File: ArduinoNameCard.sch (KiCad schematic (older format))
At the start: 24 parts, among them J1 Conn_01x05, J2 Conn_01x04, J3 Conn_01x06, J4 Conn_01x08, J5 Conn_01x06, SW1 SW_Push, U1 FT232RL, U2 MCU-ATMEGA328P-AU(TQFP32)

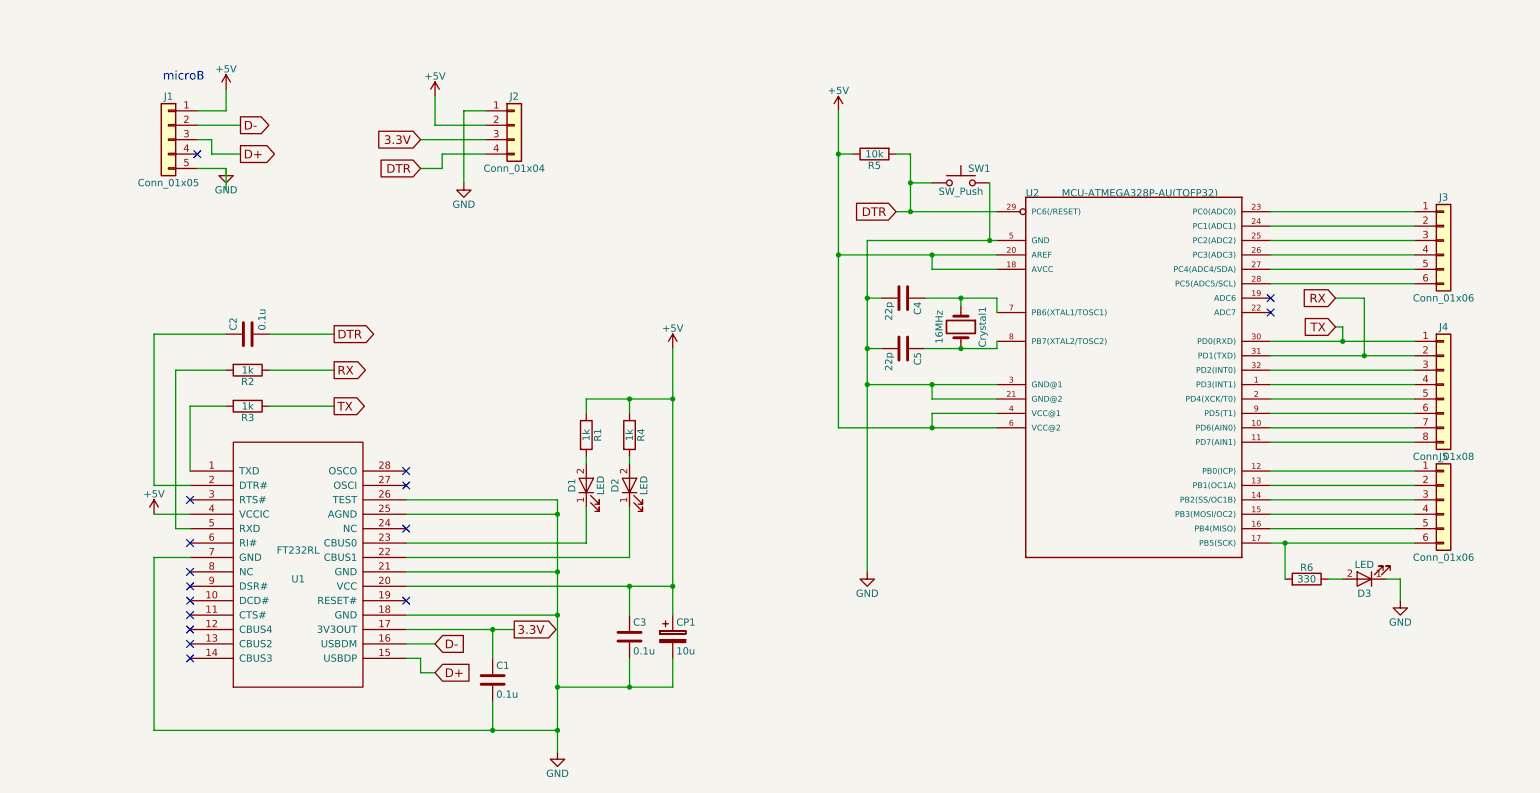
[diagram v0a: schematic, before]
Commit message: ・README.mdの追加 ・PCBの設計 諸変更を行った。
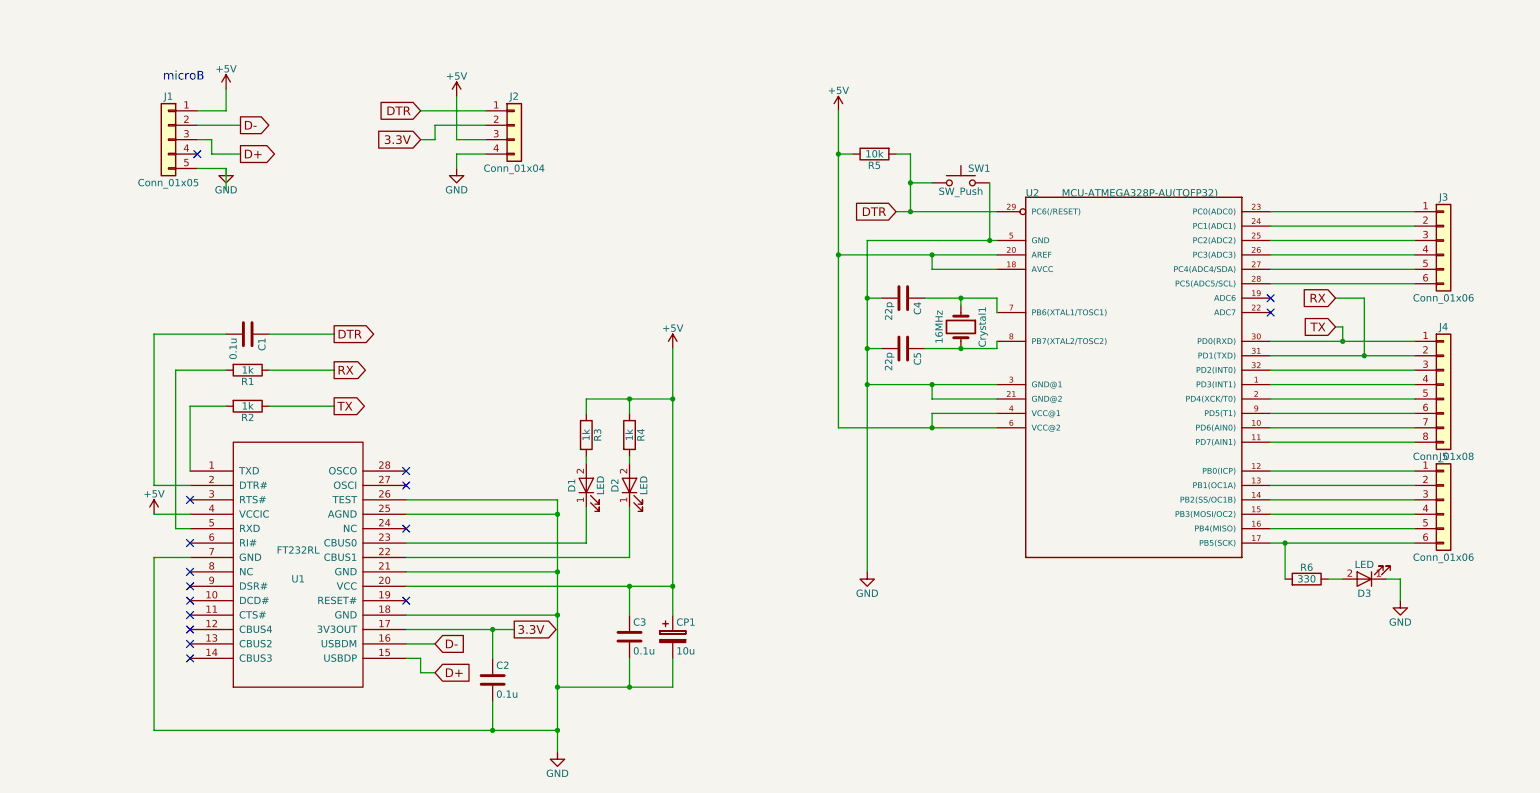
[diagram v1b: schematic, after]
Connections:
- net +5V: now also J2.3 (Pin_3), R3.1; no longer J2.2 (Pin_2), R1.1
- net 3.3V: now also C2.1, J2.2 (Pin_2); no longer C1.1, J2.3 (Pin_3)
- net DTR: now also C1.1, J2.1 (Pin_1); no longer C2.2, J2.4 (Pin_4)
- net GND: now also C2.2, J2.4 (Pin_4); no longer C1.2, J2.1 (Pin_1)
- net RX: now also R1.1; no longer R2.1
- net TX: now also R2.1; no longer R3.1
- net at U1.1 (TXD): now also R2.2; no longer R3.2
- net at U1.2 (DTR#): now also C1.2; no longer C2.1
- net at U1.5 (RXD): now also R1.2; no longer R2.2
- net at D1.2 (A): now also R3.2; no longer R1.2
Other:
- moved on the sheet: C1, C2, R1, R2, R3
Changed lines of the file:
@@
 L R R1
 U 1 1 598D7C3A
-P 4700 4200
-F 0 "R1" V 4780 4200 50  0000 C CNN
-F 1 "1k" V 4700 4200 50  0000 C CNN
-F 2 "Resistors_SMD:R_0805_HandSoldering" V 4630 4200 50  0001 C CNN
-F 3 "" H 4700 4200 50  0001 C CNN
-	1    4700 4200
-	1    0    0    -1
+P 2350 3750
+F 0 "R1" V 2430 3750 50  0000 C CNN
+F 1 "1k" V 2350 3750 50  0000 C CNN
+F 2 "Resistors_SMD:R_0805_HandSoldering" V 2280 3750 50  0001 C CNN
+F 3 "" H 2350 3750 50  0001 C CNN
+	1    2350 3750
+	0    1    1    0
 $EndComp
 $Comp
@@
 L C C1
 U 1 1 598D853B
-P 4050 5900
-F 0 "C1" H 4075 6000 50  0000 L CNN
-F 1 "0.1u" H 4075 5800 50  0000 L CNN
-F 2 "Capacitors_SMD:C_0805_HandSoldering" H 4088 5750 50  0001 C CNN
-F 3 "" H 4050 5900 50  0001 C CNN
-	1    4050 5900
-	1    0    0    -1
+P 2350 3500
+F 0 "C1" H 2375 3600 50  0000 L CNN
+F 1 "0.1u" H 2375 3400 50  0000 L CNN
+F 2 "Capacitors_SMD:C_0805_HandSoldering" H 2388 3350 50  0001 C CNN
+F 3 "" H 2350 3500 50  0001 C CNN
+	1    2350 3500
+	0    1    1    0
 $EndComp
 Text GLabel 4200 5550 2    60   Output ~ 0
@@
 L R R2
 U 1 1 598DA5A4
-P 2350 3750
-F 0 "R2" V 2430 3750 50  0000 C CNN
-F 1 "1k" V 2350 3750 50  0000 C CNN
-F 2 "Resistors_SMD:R_0805_HandSoldering" V 2280 3750 50  0001 C CNN
-F 3 "" H 2350 3750 50  0001 C CNN
-	1    2350 3750
-	0    1    1    0
-$EndComp
-$Comp
-L R R3
-U 1 1 598DA689
 P 2350 4000
-F 0 "R3" V 2430 4000 50  0000 C CNN
+F 0 "R2" V 2430 4000 50  0000 C CNN
 F 1 "1k" V 2350 4000 50  0000 C CNN
 F 2 "Resistors_SMD:R_0805_HandSoldering" V 2280 4000 50  0001 C CNN
@@
 $EndComp
 $Comp
+L R R3
+U 1 1 598DA689
+P 4700 4200
+F 0 "R3" V 4780 4200 50  0000 C CNN
+F 1 "1k" V 4700 4200 50  0000 C CNN
+F 2 "Resistors_SMD:R_0805_HandSoldering" V 4630 4200 50  0001 C CNN
+F 3 "" H 4700 4200 50  0001 C CNN
+	1    4700 4200
+	1    0    0    -1
+$EndComp
+$Comp
 L C C2
 U 1 1 598DA6BD
-P 2350 3500
-F 0 "C2" H 2375 3600 50  0000 L CNN
-F 1 "0.1u" H 2375 3400 50  0000 L CNN
-F 2 "Capacitors_SMD:C_0805_HandSoldering" H 2388 3350 50  0001 C CNN
-F 3 "" H 2350 3500 50  0001 C CNN
-	1    2350 3500
-	0    -1   -1   0
+P 4050 5900
+F 0 "C2" H 4075 6000 50  0000 L CNN
+F 1 "0.1u" H 4075 5800 50  0000 L CNN
+F 2 "Capacitors_SMD:C_0805_HandSoldering" H 4088 5750 50  0001 C CNN
+F 3 "" H 4050 5900 50  0001 C CNN
+	1    4050 5900
+	1    0    0    -1
 $EndComp
 NoConn ~ 1950 5450
@@
 L GND #PWR08
 U 1 1 5AC81876
-P 3850 2450
-F 0 "#PWR08" H 3850 2200 50  0001 C CNN
-F 1 "GND" H 3850 2300 50  0000 C CNN
-F 2 "" H 3850 2450 50  0001 C CNN
-F 3 "" H 3850 2450 50  0001 C CNN
-	1    3850 2450
+P 3800 2350
+F 0 "#PWR08" H 3800 2100 50  0001 C CNN
+F 1 "GND" H 3800 2200 50  0000 C CNN
+F 2 "" H 3800 2350 50  0001 C CNN
+F 3 "" H 3800 2350 50  0001 C CNN
+	1    3800 2350
 	1    0    0    -1
 $EndComp
@@
 L +5V #PWR09
 U 1 1 5AC818BA
-P 3650 1850
-F 0 "#PWR09" H 3650 1700 50  0001 C CNN
-F 1 "+5V" H 3650 1990 50  0000 C CNN
-F 2 "" H 3650 1850 50  0001 C CNN
-F 3 "" H 3650 1850 50  0001 C CNN
-	1    3650 1850
+P 3800 1850
+F 0 "#PWR09" H 3800 1700 50  0001 C CNN
+F 1 "+5V" H 3800 1990 50  0000 C CNN
+F 2 "" H 3800 1850 50  0001 C CNN
+F 3 "" H 3800 1850 50  0001 C CNN
+	1    3800 1850
 	1    0    0    -1
 $EndComp
@@
 	1    0    0    -1
 $EndComp
-Text GLabel 3550 2350 0    60   Input ~ 0
+Text GLabel 3550 1950 0    60   Input ~ 0
 DTR
 Wire Wire Line
-	7050 3250 7300 3250
-Wire Wire Line
-	7300 3250 7550 3250
+	7050 3250 7550 3250
 Wire Wire Line
 	7550 3250 7550 3350
@@
 	6950 2450 7100 2450
 Wire Wire Line
-	6950 2250 6950 2450
-Wire Wire Line
-	6950 2450 6950 2650
+	6950 2250 6950 2650
 Connection ~ 6450 2250
 Wire Wire Line
-	6450 1950 6450 2250
-Wire Wire Line
-	6450 2250 6450 2950
-Wire Wire Line
-	6450 2950 6450 4150
+	6450 1950 6450 4150
 Wire Wire Line
 	6450 2250 6550 2250
@@
 Connection ~ 6450 2950
 Wire Wire Line
-	6450 2950 7100 2950
-Wire Wire Line
-	7100 2950 7550 2950
-Wire Wire Line
-	6650 2850 7500 2850
-Wire Wire Line
-	7500 2850 7550 2850
+	6450 2950 7550 2950
+Wire Wire Line
+	6650 2850 7550 2850
 Connection ~ 7100 3850
 Wire Wire Line
@@
 	7550 3950 7100 3950
 Wire Wire Line
-	6650 2850 6650 3250
-Wire Wire Line
-	6650 3250 6650 3600
-Wire Wire Line
-	6650 3600 6650 3850
-Wire Wire Line
-	6650 3850 6650 5150
-Wire Wire Line
-	6650 3850 7100 3850
-Wire Wire Line
-	7100 3850 7550 3850
+	6650 2850 6650 5150
+Wire Wire Line
+	6650 3850 7550 3850
 Connection ~ 7100 4150
 Wire Wire Line
@@
 	7100 4150 7100 4050
 Wire Wire Line
-	6450 4150 7100 4150
-Wire Wire Line
-	7100 4150 7550 4150
-Wire Wire Line
-	6850 2650 6950 2650
-Wire Wire Line
-	6950 2650 7550 2650
+	6450 4150 7550 4150
+Wire Wire Line
+	6850 2650 7550 2650
 Wire Wire Line
 	1850 3750 2200 3750
@@
 Connection ~ 4050 5550
 Wire Wire Line
-	3450 5550 4050 5550
-Wire Wire Line
-	4050 5550 4200 5550
+	3450 5550 4200 5550
 Connection ~ 4050 6250
 Wire Wire Line
@@
 Connection ~ 4500 5950
 Wire Wire Line
-	4500 5950 5000 5950
-Wire Wire Line
-	5000 5950 5300 5950
+	4500 5950 5300 5950
 Wire Wire Line
 	5000 5750 5000 5950
@@
 Connection ~ 5000 3950
 Wire Wire Line
-	5300 5250 5000 5250
-Wire Wire Line
-	5000 5250 3450 5250
-Wire Wire Line
-	5300 3600 5300 3950
-Wire Wire Line
-	5300 3950 5300 5250
-Wire Wire Line
-	5300 5250 5300 5450
+	5300 5250 3450 5250
+Wire Wire Line
+	5300 3600 5300 5450
 Connection ~ 4500 6250
 Wire Wire Line
@@
 	4500 5150 3450 5150
 Wire Wire Line
-	1700 6250 4050 6250
-Wire Wire Line
-	4050 6250 4500 6250
-Wire Wire Line
-	4500 4650 4500 4750
-Wire Wire Line
-	4500 4750 4500 5150
-Wire Wire Line
-	4500 5150 4500 5450
-Wire Wire Line
-	4500 5450 4500 5950
-Wire Wire Line
-	4500 5950 4500 6250
-Wire Wire Line
-	4500 6250 4500 6400
+	4500 6250 1700 6250
+Wire Wire Line
+	4500 4650 4500 6400
 Wire Wire Line
 	4500 5450 3450 5450
@@
 	4700 3950 4700 4050
 Wire Wire Line
-	4700 3950 5000 3950
-Wire Wire Line
-	5000 3950 5300 3950
+	4700 3950 5300 3950
 Wire Wire Line
 	5000 4400 5000 4350
@@
 	7550 3600 7550 3550
 Wire Wire Line
-	7050 3600 7300 3600
-Wire Wire Line
-	7300 3600 7550 3600
+	7050 3600 7550 3600
 Wire Wire Line
 	7300 3300 7300 3250
@@
 Connection ~ 6650 3600
 Wire Wire Line
-	9450 3550 9950 3550
-Wire Wire Line
-	9950 3550 10450 3550
-Wire Wire Line
-	9450 3650 10100 3650
-Wire Wire Line
-	10100 3650 10450 3650
+	9450 3550 10450 3550
+Wire Wire Line
+	9450 3650 10450 3650
 Wire Wire Line
 	9450 3750 10450 3750
@@
 Wire Wire Line
 	10450 3150 9450 3150
-Wire Wire Line
-	3850 1950 4000 1950
-Wire Wire Line
-	3650 2050 4000 2050
-Wire Wire Line
-	3550 2150 4000 2150
 Connection ~ 7300 3600
 Wire Wire Line
@@
 Connection ~ 6650 3850
 Wire Wire Line
-	3650 2050 3650 1850
-Wire Wire Line
-	3850 1950 3850 2450
-Wire Wire Line
-	9450 4950 9550 4950
-Wire Wire Line
-	9550 4950 10450 4950
+	9450 4950 10450 4950
 Wire Wire Line
 	9550 4950 9550 5200
@@
 	10250 5200 10350 5200
 Wire Wire Line
-	4000 2250 3700 2250
-Wire Wire Line
-	3700 2250 3700 2350
-Wire Wire Line
-	3700 2350 3550 2350
+	4000 2250 3800 2250
+Wire Wire Line
+	3800 2250 3800 2350
 Wire Wire Line
 	6850 2250 6950 2250
@@
 	1    0    0    -1
 $EndComp
+Wire Wire Line
+	3550 1950 4000 1950
+Wire Wire Line
+	3550 2150 3650 2150
+Wire Wire Line
+	3650 2150 3650 2050
+Wire Wire Line
+	3650 2050 4000 2050
+Wire Wire Line
+	4000 2150 3800 2150
+Wire Wire Line
+	3800 2150 3800 1850
 $EndSCHEMATC

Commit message: 回路にヒューズを追加した
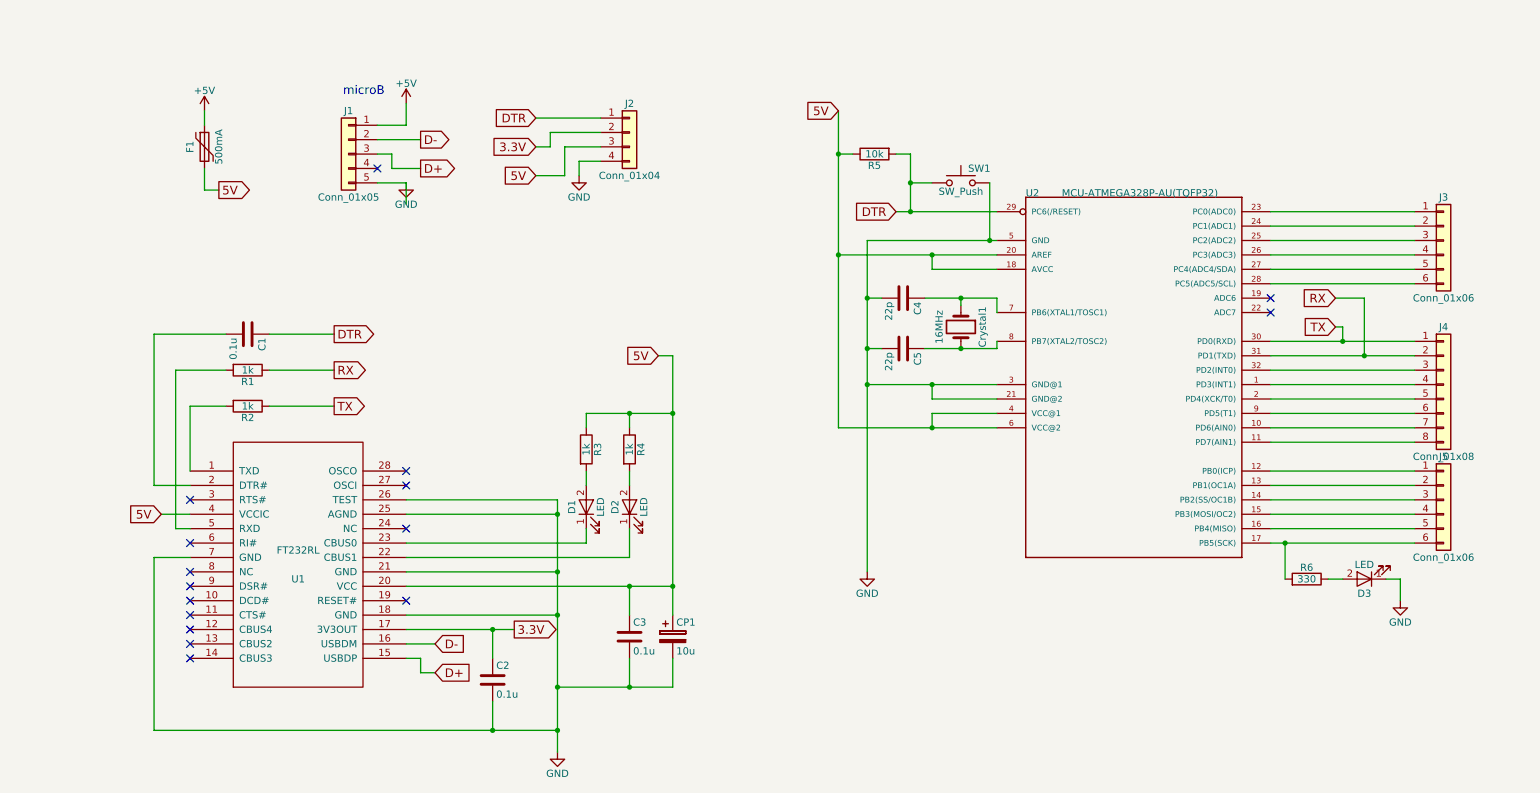
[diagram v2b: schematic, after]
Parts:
- added F1: 500mA, SMD_Packages:SMD-1210_Pol, symbol Polyfuse
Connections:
- net +5V: now also F1.1; no longer C3.1, CP1.1, J2.3 (Pin_3), R3.1, R4.1, R5.1, U1.20 (VCC), U1.4 (VCCIC), U2.18 (AVCC), U2.20 (AREF), U2.4 (VCC@1), U2.6 (VCC@2)
- new net 5V: C3.1, CP1.1, F1.2, J2.3 (Pin_3), R3.1, R4.1, R5.1, U1.20 (VCC), U1.4 (VCCIC), U2.18 (AVCC), U2.20 (AREF), U2.4 (VCC@1), U2.6 (VCC@2)
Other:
- moved on the sheet: D1, D2, J1, J2, R3, R4

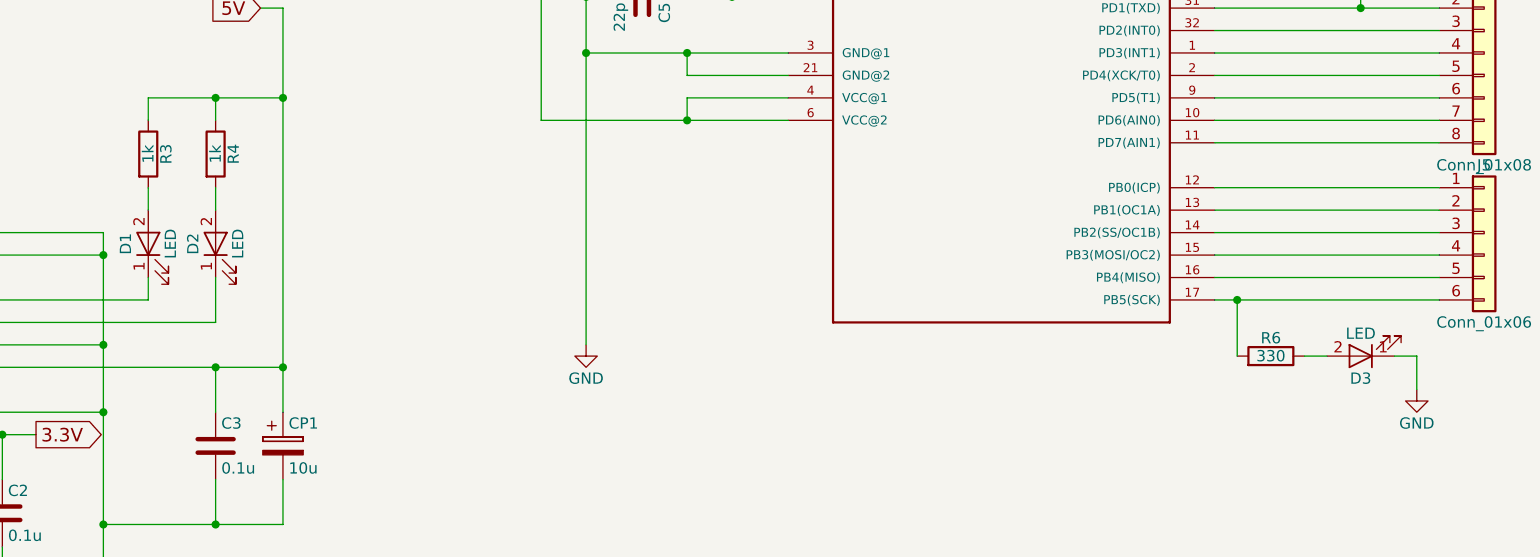
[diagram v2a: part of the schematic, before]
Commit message: LEDの種類に関する追記 部品のパラメータのシルクの追加
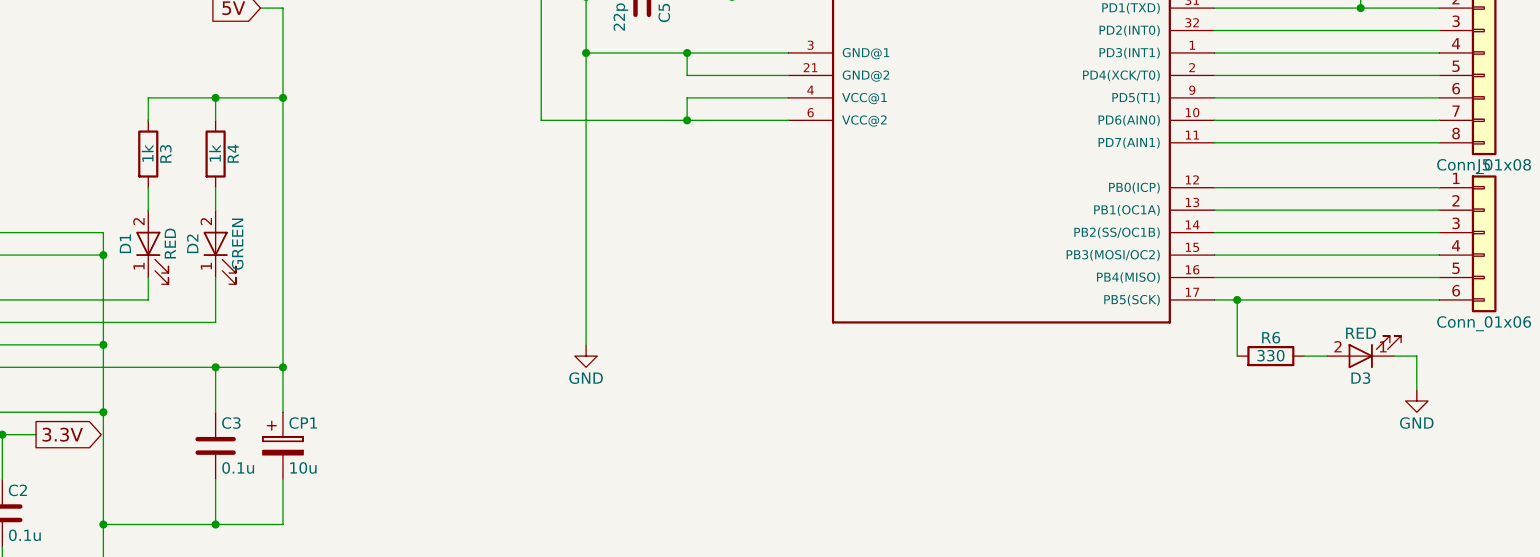
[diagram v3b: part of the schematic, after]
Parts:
- D1, D3: value LED -> RED
- D2: value LED -> GREEN
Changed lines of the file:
@@
 P 4700 4700
 F 0 "D1" H 4700 4800 50  0000 C CNN
-F 1 "LED" H 4700 4600 50  0000 C CNN
+F 1 "RED" H 4700 4600 50  0000 C CNN
 F 2 "LEDs:LED_0805_HandSoldering" H 4700 4700 50  0001 C CNN
 F 3 "" H 4700 4700 50  0001 C CNN
@@
 P 5000 4700
 F 0 "D2" H 5000 4800 50  0000 C CNN
-F 1 "LED" H 5000 4600 50  0000 C CNN
+F 1 "GREEN" H 5000 4600 50  0000 C CNN
 F 2 "LEDs:LED_0805_HandSoldering" H 5000 4700 50  0001 C CNN
 F 3 "" H 5000 4700 50  0001 C CNN
@@
 P 10100 5200
 F 0 "D3" H 10100 5300 50  0000 C CNN
-F 1 "LED" H 10100 5100 50  0000 C CNN
+F 1 "RED" H 10100 5100 50  0000 C CNN
 F 2 "LEDs:LED_0805_HandSoldering" H 10100 5200 50  0001 C CNN
 F 3 "" H 10100 5200 50  0001 C CNN

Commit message: https://github.com/DroidDIY/FT230XBreakout を参考にFT230XSに書き換えた。
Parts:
- removed C2: 0.1u, Capacitors_SMD:C_0805_HandSoldering, symbol C
- removed J1: Conn_01x05, ArduinoNameCard:namecard_microB, symbol Conn_01x05
- removed R2: 1k, Resistors_SMD:R_0805_HandSoldering, symbol R
- removed U1: FT232RL, Housings_SSOP:SSOP-28_5.3x10.2mm_Pitch0.65mm, symbol FT232RL
- added J?: USB_B_Micro, symbol Connector:USB_B_Micro
- added R?: 27, symbol Device:R
- added U?: FT230XS, symbol ArduinoNameCard:FT230XS
- C1, C4, C5: symbol C -> Device:C
- C3: symbol C -> ArduinoNameCard-rescue:C-
- CP1: symbol CP -> ArduinoNameCard-rescue:CP-
- Crystal1: symbol Crystal -> Device:Crystal
- D1, D2, D3: symbol LED -> ArduinoNameCard-rescue:LED-
- F1: symbol Polyfuse -> Device:Polyfuse
- J2: symbol Conn_01x04 -> Connector:Conn_01x04_Female
- J3, J5: symbol Conn_01x06 -> Connector:Conn_01x06_Female
- J4: symbol Conn_01x08 -> Connector:Conn_01x08_Female
- R1: value 1k -> 27; symbol R -> Device:R
- R3, R4: symbol R -> ArduinoNameCard-rescue:R-
- R5, R6: symbol R -> Device:R
- SW1: symbol SW_Push -> Switch:SW_Push
- U2: symbol MCU-ATMEGA328P-AU(TQFP32) -> ArduinoNameCard:MCU-ATMEGA328P-AU(TQFP32)
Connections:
- net labels added: 3V3, RTS
- net labels removed: 3.3V, DTR
- wire segments 116 -> 139
- no-connect marks 16 -> 7
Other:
- note removed: "microB\n"
- moved on the sheet: C1, C5, R1, R6, SW1
